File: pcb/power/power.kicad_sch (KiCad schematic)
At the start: 19 parts, among them J401 Barrel_Jack_Switch, U401 TPS62933

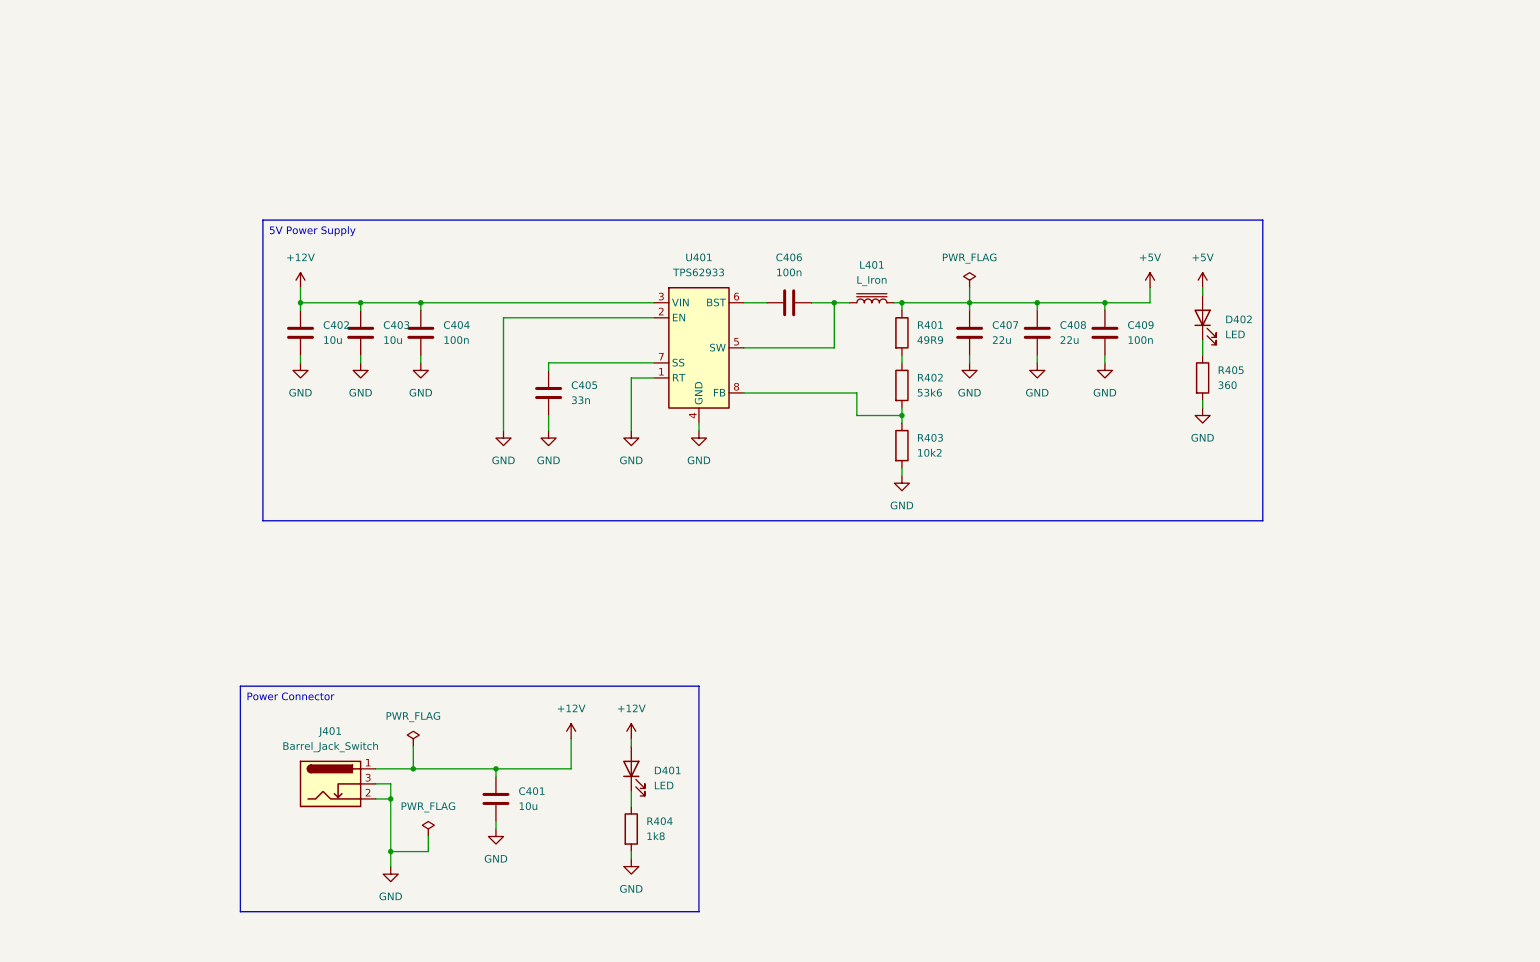
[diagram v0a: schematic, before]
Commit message: add power pcb
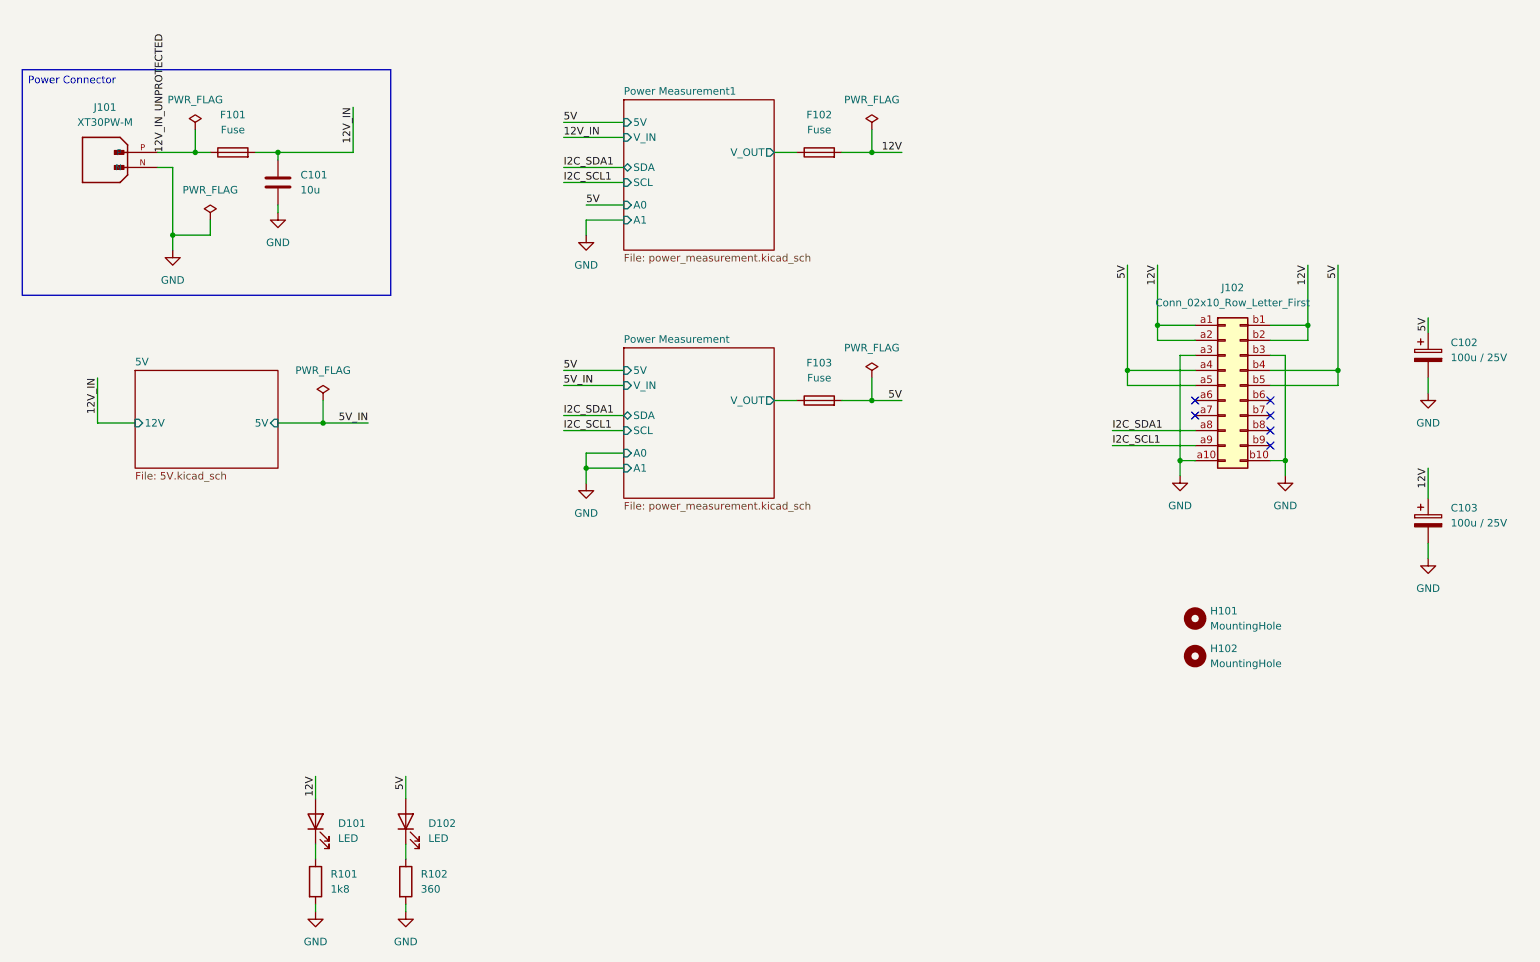
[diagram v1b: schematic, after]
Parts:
- removed C402, C403: 10u, symbol Device:C
- removed C404, C406, C409: 100n, symbol Device:C
- removed C405: 33n, symbol Device:C
- removed C407, C408: 22u, symbol Device:C
- removed J401: Barrel_Jack_Switch, Connector_BarrelJack:BarrelJack_GCT_DCJ200-10-A_Horizontal, symbol Connector:Barrel_Jack_Switch
- removed L401: L_Iron, symbol Device:L_Iron
- removed R401: 49R9, Resistor_SMD:R_0805_2012Metric, symbol Device:R
- removed R402: 53k6, Resistor_SMD:R_0805_2012Metric, symbol Device:R
- removed R403: 10k2, Resistor_SMD:R_0805_2012Metric, symbol Device:R
- removed U401: TPS62933, Package_TO_SOT_SMD:SOT-583-8, symbol Regulator_Switching:TPS62933
- added C102, C103: 100u / 25V, Capacitor_Tantalum_SMD:CP_EIA-7343-43_Kemet-X_Pad2.25x2.55mm_HandSolder, symbol Device:C_Polarized
- added F101, F102, F103: Fuse, PRJ:Fuseholder, symbol Device:Fuse
- added H101, H102: MountingHole, MountingHole:MountingHole_3.2mm_M3, symbol Mechanical:MountingHole
- added J101: XT30PW-M, PRJ:XT30PW-M, symbol XT30PW-M:XT30PW-M
- added J102: Conn_02x10_Row_Letter_First, PRJ:PCN10C-20S-2.54DS, symbol Connector_Generic:Conn_02x10_Row_Letter_First
- C101: renamed from C401; footprint (none) -> Capacitor_SMD:C_1206_3216Metric
- D101: renamed from D401; footprint (none) -> LED_SMD:LED_0805_2012Metric
- D102: renamed from D402; footprint (none) -> LED_SMD:LED_0805_2012Metric
- R101: renamed from R404; footprint (none) -> Resistor_SMD:R_0805_2012Metric
- R102: renamed from R405; footprint (none) -> Resistor_SMD:R_0805_2012Metric
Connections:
- net GND: now also C102.2, C103.2, J101.N, J102.a10 (Pin_a10), J102.a3 (Pin_a3), J102.b10 (Pin_b10), J102.b3 (Pin_b3)
- net +12V renamed 12V
- net 12V: now also C103.1, F102.2, J102.a1 (Pin_a1), J102.a2 (Pin_a2), J102.b1 (Pin_b1), J102.b2 (Pin_b2); no longer C101.1
- net +5V renamed 5V
- net 5V: now also C102.1, F103.2, J102.a4 (Pin_a4), J102.a5 (Pin_a5), J102.b4 (Pin_b4), J102.b5 (Pin_b5)
- new net 12V_IN: C101.1, F101.2
- new net 12V_IN_UNPROTECTED: F101.1, J101.P
- new net I2C_SCL1: J102.a9 (Pin_a9)
- new net I2C_SDA1: J102.a8 (Pin_a8)
- new net Power Measurement/V_OUT: F103.1
- new net Power Measurement1/V_OUT: F102.1
- no-connect marks 0 -> 6
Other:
- added sheet 5V (5V.kicad_sch)
- added sheet Power Measurement (power_measurement.kicad_sch)
- added sheet Power Measurement1 (power_measurement.kicad_sch)
- company: Amateurfunkclub für Remote Stationen -> (none)
- title: Power -> (none)
- moved on the sheet: C101, D101, D102, R101, R102

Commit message: update
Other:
- moved on the sheet: C101, F101, J101

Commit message: update
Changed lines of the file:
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@@
+	)
+	(junction
+		(at 52.07 39.37)
+		(diameter 0)
+		(color 0 0 0 0)
 	)
 	(junction
@@
 	(wire
 		(pts
+			(xy 52.07 39.37) (xy 53.34 39.37)
+		)
+		(stroke
+			(width 0)
+			(type default)
+		)
+	)
+	(wire
+		(pts
 			(xy 113.03 81.28) (xy 123.19 81.28)
 		)
@@
 	(wire
 		(pts
-			(xy 44.45 39.37) (xy 53.34 39.37)
+			(xy 44.45 39.37) (xy 52.07 39.37)
 		)
 		(stroke
@@
 		(pts
 			(xy 116.84 85.09) (xy 116.84 87.63)
+		)
+		(stroke
+			(width 0)
+			(type default)
+		)
+	)
+	(wire
+		(pts
+			(xy 52.07 34.29) (xy 52.07 39.37)
 		)
 		(stroke
@@
 	)
 	(label "12V_IN_UNPROTECTED"
-		(at 49.53 39.37 90)
+		(at 46.99 39.37 90)
 		(effects
 			(font
@@
 					(unit 1)
 				)
+			)
+		)
+	)
+	(symbol
+		(lib_id "power:PWR_FLAG")
+		(at 52.07 34.29 0)
+		(unit 1)
+		(exclude_from_sim no)
+		(in_bom yes)
+		(on_board yes)
+		(dnp no)
+		(fields_autoplaced yes)
+		(property "Reference" "#FLG0106"
+			(at 52.07 32.385 0)
+			(effects
+				(font
+					(size 1.27 1.27)
+				)
+				(hide yes)
+			)
+		)
+		(property "Value" "PWR_FLAG"
+			(at 52.07 29.21 0)
+			(effects
+				(font
+					(size 1.27 1.27)
+				)
+			)
+		)
+		(property "Footprint" ""
+			(at 52.07 34.29 0)
+			(effects
+				(font
+					(size 1.27 1.27)
+				)
+				(hide yes)
+			)
+		)
+		(property "Datasheet" "~"
+			(at 52.07 34.29 0)
+			(effects
+				(font
+					(size 1.27 1.27)
+				)
+				(hide yes)
+			)
+		)
+		(property "Description" "Special symbol for telling ERC where power comes from"
+			(at 52.07 34.29 0)
+			(effects
+				(font
+					(size 1.27 1.27)
+				)
+				(hide yes)
+			)
+		)
+		(pin "1"
+		)
+		(instances
+			(project "power"
+				(path "/f29935ff-76ad-48dd-a9d8-f60fd99054e1"
+					(reference "#FLG0106")
+					(unit 1)
+				)

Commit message: update ALL parts
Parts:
- C101: LCSC (none) -> C13585
- C102, C103: footprint Capacitor_Tantalum_SMD:CP_EIA-7343-43_Kemet-X_Pad2.25x2.55mm_HandSolder -> Capacitor_Tantalum_SMD:CP_EIA-7343-43_Kemet-X; LCSC C7230 -> C132558
- D101, D102: LCSC (none) -> C84256
- J102: MOUSER (none) -> 798-PCN10C20S254DS72
- R101: value 1k8 -> 2k2; LCSC (none) -> C17520
- R102: value 360 -> 1k; LCSC (none) -> C17513
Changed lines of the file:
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@@
 			)
 		)
-		(property "Footprint" "Capacitor_Tantalum_SMD:CP_EIA-7343-43_Kemet-X_Pad2.25x2.55mm_HandSolder"
+		(property "Footprint" "Capacitor_Tantalum_SMD:CP_EIA-7343-43_Kemet-X"
 			(at 260.0452 72.39 0)
 			(effects
@@
 			)
 		)
-		(property "LCSC" "C7230"
+		(property "LCSC" "C132558"
 			(at 259.08 68.58 0)
 			(effects
@@
 				)
 				(hide yes)
+			)
+		)
+		(property "MOUSER" ""
+			(at 259.08 68.58 0)
+			(effects
+				(font
+					(size 1.27 1.27)
+				)
 			)
 		)
@@
 			)
 		)
-		(property "LCSC" ""
+		(property "LCSC" "C84256"
 			(at 86.36 147.32 0)
 			(effects
@@
 			)
 		)
+		(property "MOUSER" ""
+			(at 86.36 147.32 0)
+			(effects
+				(font
+					(size 1.27 1.27)
+				)
+			)
+		)
 		(pin "2"
 		)
@@
 			)
 		)
+		(property "MOUSER" ""
+			(at 219.71 113.03 0)
+			(effects
+				(font
+					(size 1.27 1.27)
+				)
+			)
+		)
 		(instances
 			(project "power"
@@
 			)
 		)
-		(property "LCSC" ""
+		(property "LCSC" "C84256"
 			(at 71.12 147.32 0)
 			(effects
@@
 			)
 		)
+		(property "MOUSER" ""
+			(at 71.12 147.32 0)
+			(effects
+				(font
+					(size 1.27 1.27)
+				)
+			)
+		)
 		(pin "2"
 		)
@@
 			)
 		)
-		(property "Value" "360"
+		(property "Value" "1k"
 			(at 88.9 158.7499 0)
 			(effects
@@
 			)
 		)
-		(property "LCSC" ""
+		(property "LCSC" "C17513"
 			(at 86.36 157.48 0)
 			(effects
@@
 				)
 				(hide yes)
+			)
+		)
+		(property "MOUSER" ""
+			(at 86.36 157.48 0)
+			(effects
+				(font
+					(size 1.27 1.27)
+				)
 			)
 		)
@@
 			)
 		)
-		(property "Footprint" "Capacitor_Tantalum_SMD:CP_EIA-7343-43_Kemet-X_Pad2.25x2.55mm_HandSolder"
+		(property "Footprint" "Capacitor_Tantalum_SMD:CP_EIA-7343-43_Kemet-X"
 			(at 260.0452 100.33 0)
 			(effects
@@
 			)
 		)
-		(property "LCSC" "C7230"
+		(property "LCSC" "C132558"
 			(at 259.08 96.52 0)
 			(effects
@@
 				)
 				(hide yes)
+			)
+		)
+		(property "MOUSER" ""
+			(at 259.08 96.52 0)
+			(effects
+				(font
+					(size 1.27 1.27)
+				)
 			)
 		)
@@
 			)
 		)
+		(property "MOUSER" ""
+			(at 39.37 39.37 0)
+			(effects
+				(font
+					(size 1.27 1.27)
+				)
+			)
+		)
 		(pin "N"
 		)
@@
 			)
 		)
+		(property "MOUSER" ""
+			(at 156.21 34.29 0)
+			(effects
+				(font
+					(size 1.27 1.27)
+				)
+			)
+		)
 		(pin "2"
 		)
@@
 			)
 		)
+		(property "MOUSER" ""
+			(at 57.15 39.37 0)
+			(effects
+				(font
+					(size 1.27 1.27)
+				)
+			)
+		)
 		(pin "2"
 		)
@@
 			)
 		)
-		(property "Value" "1k8"
+		(property "Value" "2k2"
 			(at 73.66 158.7499 0)
 			(effects
@@
 			)
 		)
-		(property "LCSC" ""
+		(property "LCSC" "C17520"
 			(at 71.12 157.48 0)
 			(effects
@@
 				)
 				(hide yes)
+			)
+		)
+		(property "MOUSER" ""
+			(at 71.12 157.48 0)
+			(effects
+				(font
+					(size 1.27 1.27)
+				)
 			)
 		)
@@
 			)
 		)
+		(property "MOUSER" "798-PCN10C20S254DS72"
+			(at 224.79 73.66 0)
+			(effects
+				(font
+					(size 1.27 1.27)
+				)
+				(hide yes)
+			)
+		)
 		(pin "a5"
 		)
@@
 			)
 		)
+		(property "MOUSER" ""
+			(at 219.71 119.38 0)
+			(effects
+				(font
+					(size 1.27 1.27)
+				)
+			)
+		)
 		(instances
 			(project "power"
@@
 			)
 		)
-		(property "LCSC" ""
+		(property "LCSC" "C13585"
 			(at 64.77 44.45 0)
 			(effects
@@
 				)
 				(hide yes)
+			)
+		)
+		(property "MOUSER" ""
+			(at 64.77 44.45 0)
+			(effects
+				(font
+					(size 1.27 1.27)
+				)
 			)
 		)
@@
 			)
 		)
+		(property "MOUSER" ""
+			(at 156.21 76.2 0)
+			(effects
+				(font
+					(size 1.27 1.27)
+				)
+			)
+		)

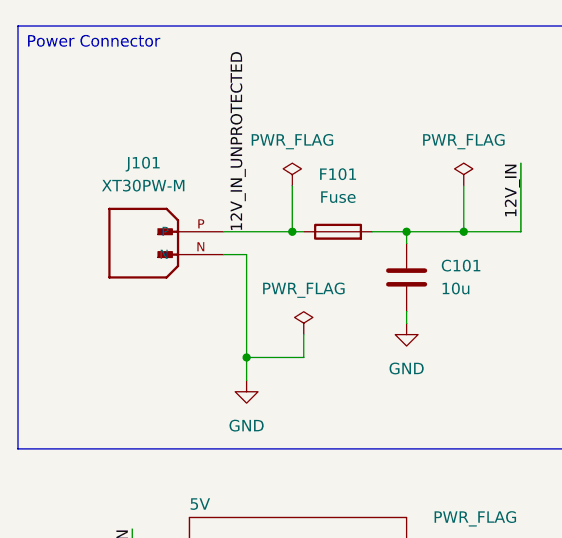
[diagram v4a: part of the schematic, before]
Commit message: update XT30 to XT60 connector
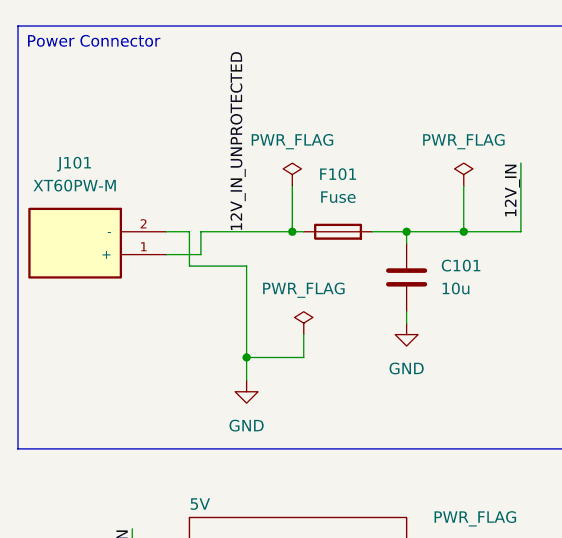
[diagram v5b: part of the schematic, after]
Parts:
- removed J101: XT30PW-M, PRJ:XT30PW-M, symbol XT30PW-M:XT30PW-M
- added J101: XT60PW-M, PRJ:AMASS_XT60PW-M, symbol XT60PW-M:XT60PW-M
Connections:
- net 12V_IN_UNPROTECTED: now also J101.1 (+)
- net GND: now also J101.2 (-)

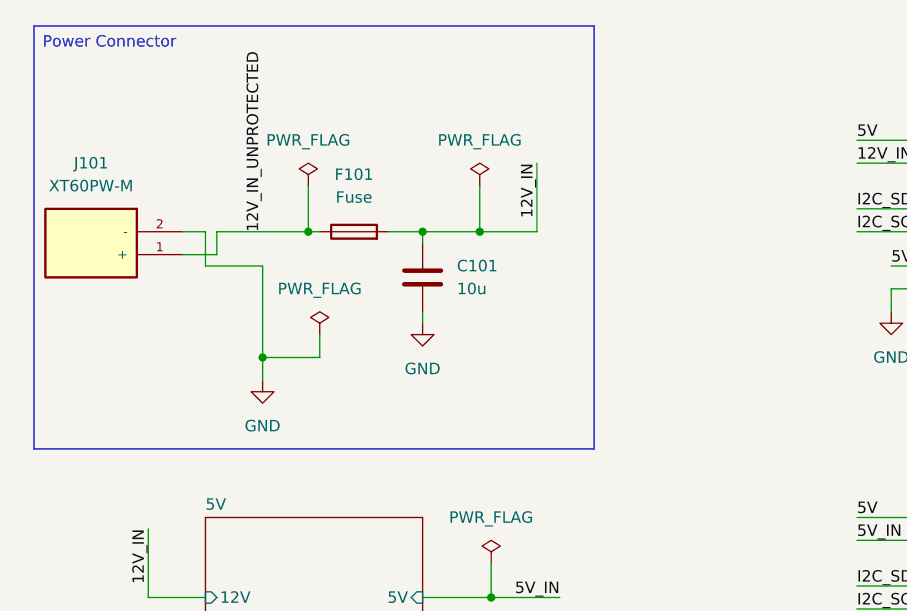
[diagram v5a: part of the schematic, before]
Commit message: update XT60 connector to official one
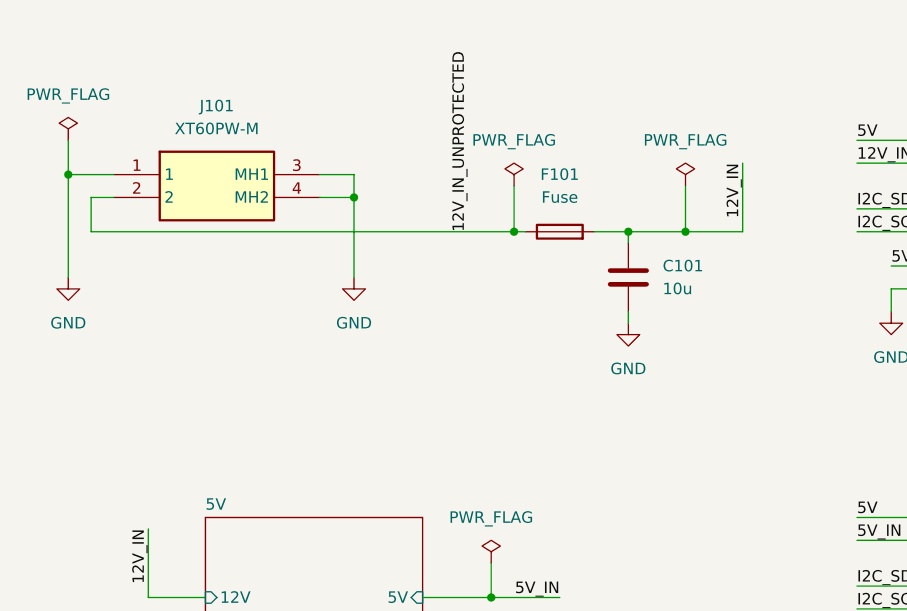
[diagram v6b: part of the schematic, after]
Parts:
- J101: footprint PRJ:AMASS_XT60PW-M -> PRJ:XT60PWM; Availability Not in stock -> (none); Check_prices https://www.snapeda.com/parts/XT60PW-M/AMASS/view-part/?ref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 -> (none); Description_1 Socket, DC supply, male, PIN: 2 -> (none); Height (none) -> 8.4; MANUFACTURER AMASS -> (none); MAXIMUM_PACKAGE_HEIGHT 8.4 mm -> (none); MF AMASS -> (none); MP XT60PW-M -> (none); Manufacturer_Name (none) -> Amass; Manufacturer_Part_Number (none) -> XT60PW-M; PARTREV V1.2 -> (none); Package Package -> (none); Price None -> (none); STANDARD Manufacturer recommendations -> (none); SnapEDA_Link https://www.snapeda.com/parts/XT60PW-M/AMASS/view-part/?ref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 -> (none)
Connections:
- net 12V_IN_UNPROTECTED: now also J101.2; no longer J101.1 (+)
- net GND: now also J101.1, J101.3 (MH1), J101.4 (MH2); no longer J101.2 (-)
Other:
- moved on the sheet: C101, F101

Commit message: update power pcb
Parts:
- F101, F102, F103: footprint PRJ:Fuseholder -> PRJ:FUSE_01530007Z
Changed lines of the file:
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@@
 			)
 		)
-		(property "Footprint" "PRJ:Fuseholder"
+		(property "Footprint" "PRJ:FUSE_01530007Z"
 			(at 156.21 36.068 90)
 			(effects
@@
 			)
 		)
-		(property "Footprint" "PRJ:Fuseholder"
+		(property "Footprint" "PRJ:FUSE_01530007Z"
 			(at 80.01 41.148 90)
 			(effects
@@
 			)
 		)
-		(property "Footprint" "PRJ:Fuseholder"
+		(property "Footprint" "PRJ:FUSE_01530007Z"
 			(at 156.21 77.978 90)
 			(effects
